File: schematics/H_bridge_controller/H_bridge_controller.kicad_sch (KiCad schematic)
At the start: 16 parts, among them J1 Conn_01x08_Male, J2 Screw_Terminal_01x02, J3 Screw_Terminal_01x02, J4 Screw_Terminal_01x02, U1 LMD18200, U2 LMD18200

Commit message: feat: updated H_bridge_controller schematics.
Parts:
- removed J1: Conn_01x08_Male, symbol Connector:Conn_01x08_Male
- removed J2: Screw_Terminal_01x02, symbol Connector:Screw_Terminal_01x02
- removed R1, R2: 10k, symbol Device:R
- added J1: Screw_Terminal_01x06, symbol Connector:Screw_Terminal_01x06
- C2, C4: value 1u -> 100n
- renumbered J3 to J2, J4 to J3
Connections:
- net +12V: now also J1.4 (Pin_4)
- net GND: now also J1.3 (Pin_3)
- net Left 1: now also J1.6 (Pin_6); no longer J2.1 (Pin_1)
- net Left 2: now also J1.5 (Pin_5); no longer J2.2 (Pin_2)
- net Left PWM: now also J2.1 (Pin_1)
- net Left direction: now also J2.2 (Pin_2)
- net Right 1: now also J1.2 (Pin_2); no longer J3.1 (Pin_1)
- net Right 2: now also J1.1 (Pin_1); no longer J3.2 (Pin_2)
- net Right PWM: now also J3.1 (Pin_1)
- net Right direction: now also J3.2 (Pin_2)
- net Error: no longer names the net of U1.9 (~{THERMAL_FLAG_OUTPUT})
- net Error: no longer U2.9 (~{THERMAL_FLAG_OUTPUT})
- net Left sense: no longer names the net of U1.8 (CURRENT_SENSE_OUTPUT)
- net Right sense: no longer names the net of U2.8 (CURRENT_SENSE_OUTPUT)
- no-connect marks 0 -> 4
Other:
- note removed: "377uA per A 377uA * 10k = 3.77V"
- note removed: "Open collector"
- moved on the sheet: J2, J3

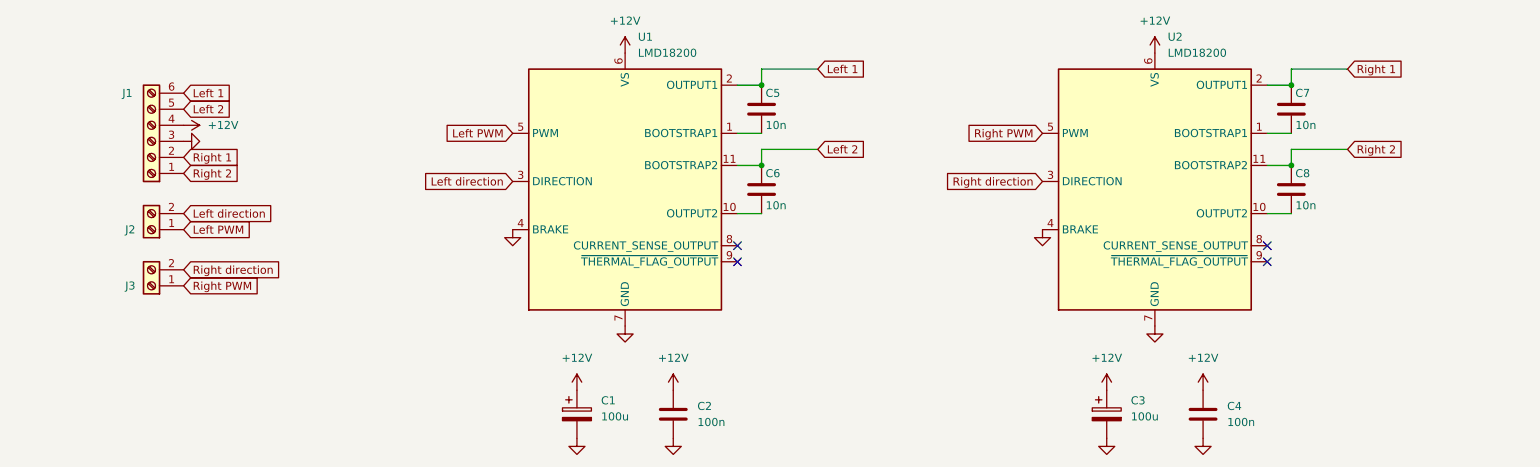
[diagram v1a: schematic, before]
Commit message: fix: added pull-down resistors to the H_bridge_controller schematics.
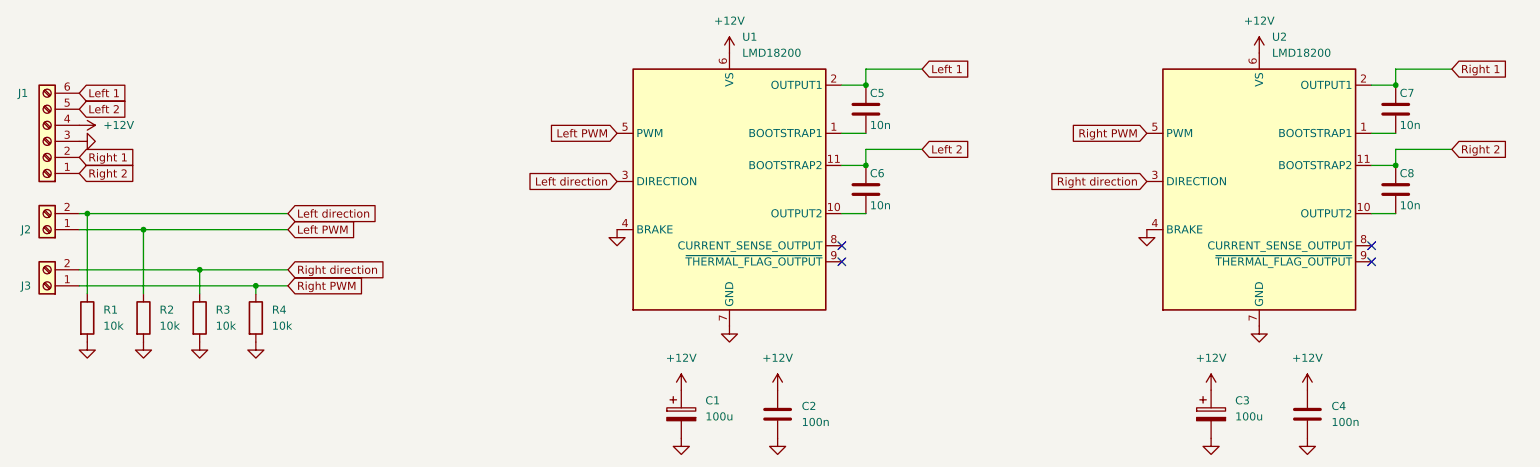
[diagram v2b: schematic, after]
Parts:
- added R1, R2, R3, R4: 10k, symbol Device:R
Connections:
- net GND: now also R1.2, R2.2, R3.2, R4.2
- net Left PWM: now also R2.1
- net Left direction: now also R1.1
- net Right PWM: now also R4.1
- net Right direction: now also R3.1
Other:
- moved on the sheet: C1, C2, C3, C4, C5, C6, C7, C8, J1, J2, J3, U1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
